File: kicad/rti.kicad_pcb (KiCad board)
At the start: 2 copper layers, 100 x 80 mm, 67 parts, among them J1 28V 250mA, J10 Grove, J2 Trigger, J3 Flash, J4 ICSP, J5 Anodes, J6 Cathodes, J7 Start, J8 Trigger, J9 Flash, Q1 BD140, Q10 BD140, Q11 BD140, Q12 BD140, Q13 BD140, Q14 BD140, Q15 BD140, Q16 BD140, Q2 BD140, Q3 BD140, Q4 BD140, Q5 BD140, Q6 BD140, Q7 BD140, Q8 BD140, Q9 BD140, SW1 Start, SW2 Reset, U1 ATMEGA328P-PU, U2 TPIC6B595, U3 TPIC6B595, U4 LM317T, U5 PC827, U6 LM7805CT, Y1 16MHz

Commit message: WIP. Add pretty picture.
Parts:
- added J11: Reset, Connectors_JST:JST_PH_B3B-PH-K_03x2.00mm_Straight, F.Cu at (235.6, 113.0)
- J2: footprint Connectors_Lumberg:1501_04 -> Connectors_Lumberg:1503_07
- moved J7 10.8 mm to (224.2, 113.0)
- moved U5 3.59 mm to (261.6, 96.5)
- moved C3 2.54 mm to (262.9, 88.9), turned to 90 degrees
- moved C4 2.54 mm to (228.6, 88.9), turned to 90 degrees
- moved G*** 2.01 mm to (215.9, 100.3)
- moved D1 2.01 mm to (211.5, 121.3)
- moved J3 1.27 mm to (245.1, 128.3)
- moved C2 1.27 mm to (174.0, 87.6), turned to 0 degrees
- moved SW2 1.27 mm to (231.1, 124.5)
- moved J8 0.63 mm to (258.4, 113.0)
- moved J9 0.63 mm to (247.0, 113.0)
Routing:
- net /D2: track 72.4 -> 90.0 mm, vias 1 -> 0
- net /D3: track 112.6 -> 98.2 mm
- net Net-(J2-Pad1): track 14.9 -> 28.1 mm
- net Net-(D1-Pad2): track 38.5 -> 28.0 mm
- net /RESET: track 84.8 -> 92.1 mm
- net /D4: track 63.7 -> 69.6 mm, vias 1 -> 0
- net Net-(J2-Pad2): track 19.8 -> 16.1 mm
- net +5V: track 177.9 -> 174.8 mm
- net Net-(R2-Pad2): track 61.4 -> 58.9 mm
- net /D5: track 98.0 -> 100.2 mm, vias 1 -> 0
- net Net-(R3-Pad2): track 56.4 -> 58.5 mm
- net /D8: track 77.9 -> 76.4 mm
- net Net-(J2-Pad3): track 19.7 -> 18.5 mm
- net /D6: track 106.1 -> 106.8 mm
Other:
- board text added: "1"
- board text added: "28V 250mA"
- board text added: "Anodes"
- board text added: "Cathodes"
- board text added: "Flash"
- board text added: "Grove"
- board text added: "ICSP"
- board text added: "Ready"
- board text added: "Reset"
- board text added: "Start"
- board text added: "Trigger"

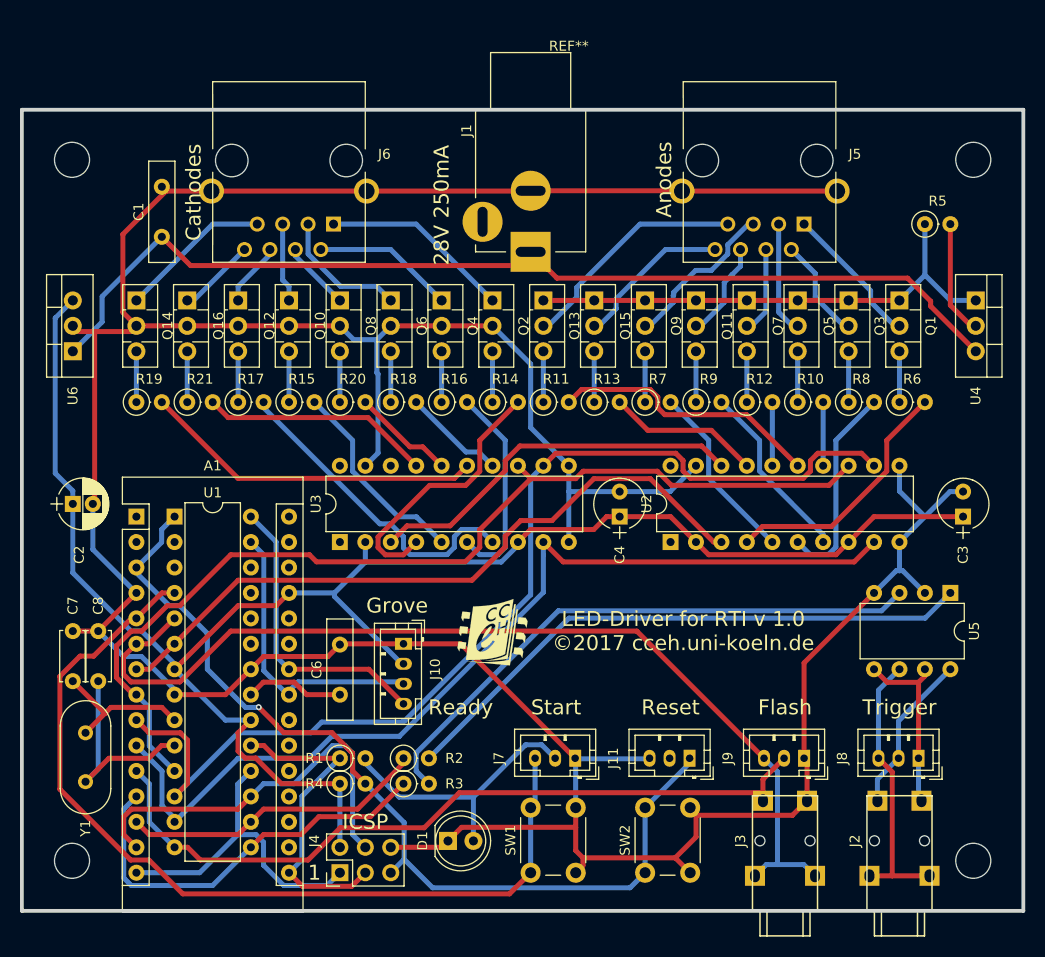
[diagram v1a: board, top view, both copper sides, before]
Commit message: Get rid of Arduino overhead.
Change program to use ATmega port names instead of Arduino.
Add ISP programming in Makefile.
Renumber and move transistors.
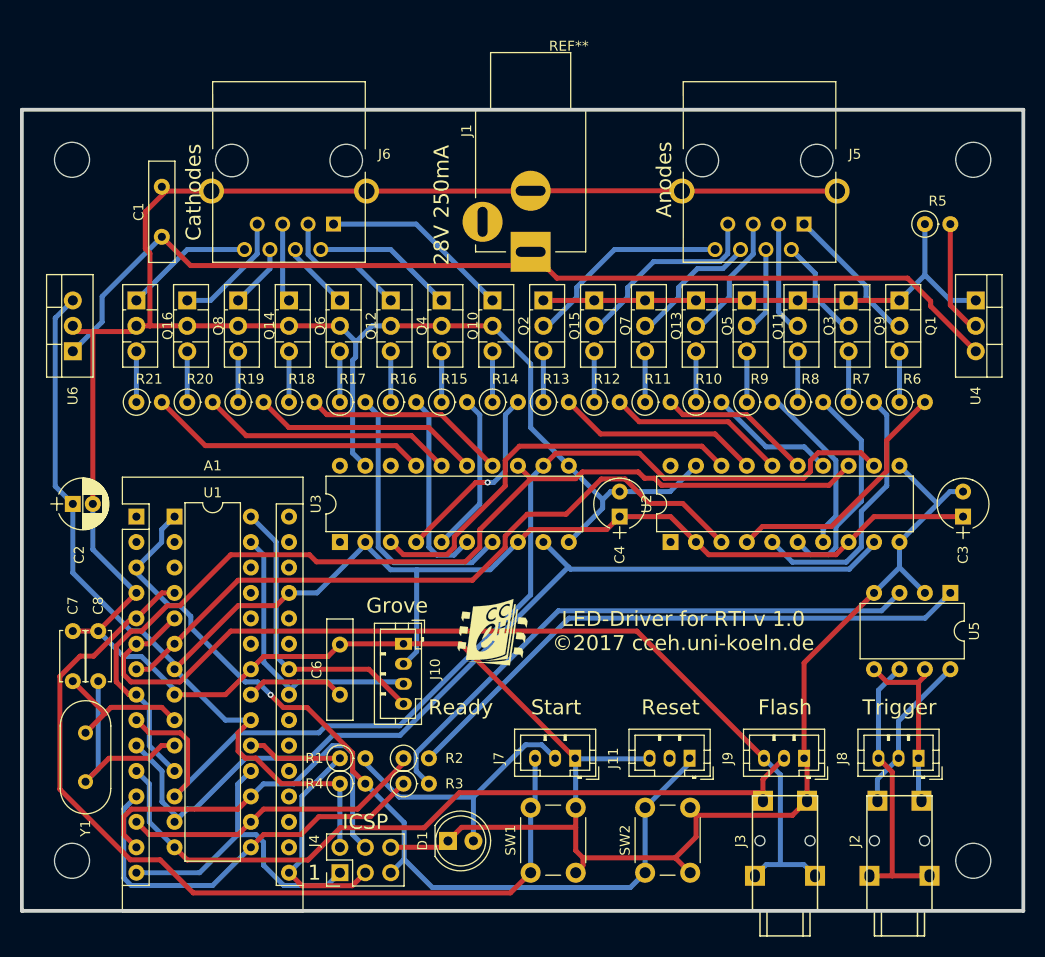
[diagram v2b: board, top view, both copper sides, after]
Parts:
- moved Q9 20.3 mm to (251.5, 67.3)
- moved R7 20.3 mm to (251.5, 77.5)
- moved Q7 15.2 mm to (226.1, 67.3)
- moved Q8 15.2 mm to (185.4, 67.3)
- moved R12 15.2 mm to (226.1, 77.5)
- moved R20 15.2 mm to (185.4, 77.5)
- moved Q10 15.2 mm to (210.8, 67.3)
- moved R15 15.2 mm to (210.8, 77.5)
- moved Q12 10.2 mm to (200.7, 67.3)
- moved Q13 10.2 mm to (231.1, 67.3)
- moved Q14 10.2 mm to (190.5, 67.3)
- moved Q5 10.2 mm to (236.2, 67.3)
- moved Q6 10.2 mm to (195.6, 67.3)
- moved R10 10.2 mm to (236.2, 77.5)
- moved R11 10.2 mm to (231.1, 77.5)
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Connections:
- Q10 pad 1: /Cat4 -> /Cat1
- Q11 pad 2: /An5 -> /An3
- Q12 pad 1: /Cat5 -> /Cat3
- Q13 pad 2: /An6 -> /An5
- Q14 pad 1: /Cat6 -> /Cat5
- Q3 pad 2: /An1 -> /An2
- Q4 pad 1: /Cat1 -> /Cat2
- Q5 pad 2: /An2 -> /An4
- Q6 pad 1: /Cat2 -> /Cat4
- Q7 pad 2: /An3 -> /An6
- Q8 pad 1: /Cat3 -> /Cat6
- Q9 pad 2: /An4 -> /An1
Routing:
- net Net-(R20-Pad2): track 10.3 -> 25.5 mm
- net Net-(R11-Pad2): track 27.2 -> 15.3 mm
- net Net-(R12-Pad2): track 6.35 -> 17.9 mm
- net Net-(R19-Pad2): track 34.2 -> 23.0 mm
- net Net-(R18-Pad2): track 10.3 -> 20.4 mm
- net Net-(R7-Pad2): track 18.2 -> 26.4 mm
- net Net-(R14-Pad2): track 27.0 -> 19.2 mm, vias 0 -> 1
- net Net-(R10-Pad2): track 6.35 -> 12.8 mm
- net /An7: track 15.8 -> 20.9 mm
- net /Cat7: track 7.82 -> 12.9 mm
- net Net-(R13-Pad2): track 15.3 -> 20.4 mm
- net Net-(R21-Pad2): track 23.0 -> 28.0 mm
- net Net-(R17-Pad2): track 32.3 -> 27.9 mm
- net Net-(R15-Pad2): track 20.3 -> 16.1 mm
- net /An5: track 9.74 -> 13.4 mm
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
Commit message: Get rid of Arduino physically. Add case. New board layout.
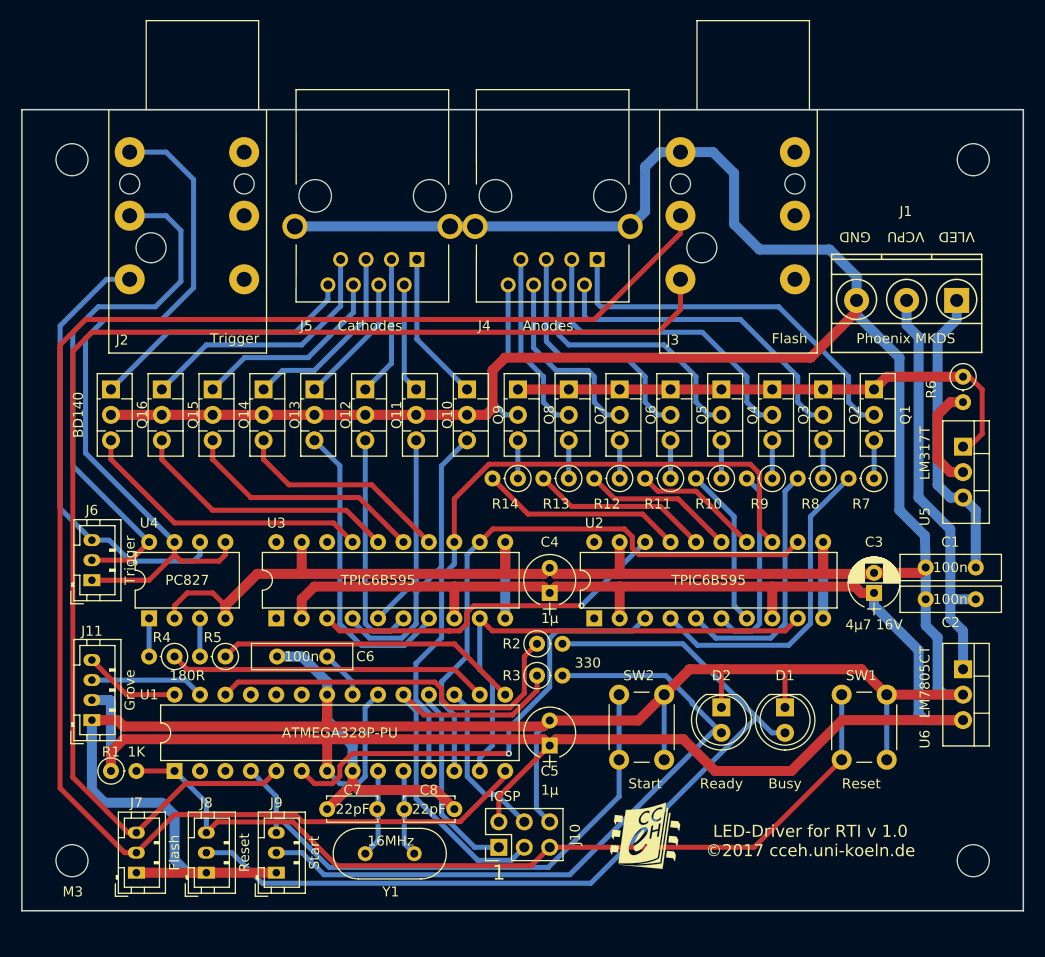
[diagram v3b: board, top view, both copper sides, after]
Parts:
- removed A1: Arduino_Nano_v3.x, Modules:Arduino_Nano
- removed the R14 at (215.9, 77.5)
- removed R15, R16, R17, R18, R19, R20, R21: 0R, Resistors_THT:R_Axial_DIN0207_L6.3mm_D2.5mm_P2.54mm_Vertical
- removed the R5 at (259.1, 59.7)
- removed REF**: EuroBoard_halb_Type-I_100mmX80mm_holes, EuroBoard_Outline:EuroBoard_halb_Type-I_100mmX80mm_holes
- added C2: 100n, Capacitors_THT:C_Disc_D10.0mm_W2.5mm_P5.00mm, F.Cu at (264.2, 97.2)
- added D1: Busy, LEDs:LED_D5.0mm, F.Cu at (245.1, 108.0)
- added M3: MountingHole_3.2mm_M3_DIN965, Mounting_Holes:MountingHole_3.2mm_M3, F.Cu at (173.9, 123.3)
- added M3_1: MountingHole_3.2mm_M3_DIN965, Mounting_Holes:MountingHole_3.2mm_M3, F.Cu at (173.9, 53.3)
- added M3_2: MountingHole_3.2mm_M3_DIN965, Mounting_Holes:MountingHole_3.2mm_M3, F.Cu at (263.9, 53.3)
- added M3_3: MountingHole_3.2mm_M3_DIN965, Mounting_Holes:MountingHole_3.2mm_M3, F.Cu at (263.9, 123.3)
- added R2: 330, Resistors_THT:R_Axial_DIN0207_L6.3mm_D2.5mm_P2.54mm_Vertical, F.Cu at (220.3, 101.6)
- added R6: 6R2 0W25, Resistors_THT:R_Axial_DIN0207_L6.3mm_D2.5mm_P2.54mm_Vertical, F.Cu at (262.9, 74.9)
- C7, C8: value 15pF -> 22pF
- J1: value 28V 250mA -> Phoenix MKDS; footprint Connectors_Anonymous:HEBG9_21 -> Connectors_Terminal_Blocks:TerminalBlock_Pheonix_MKDS1.5-3pol
- J2, J3: footprint Connectors_Lumberg:1503_07 -> Connectors_Neutrik:NRJ6HF
- R3: renamed from R1; value 1K -> 330
- moved J2 106.1 mm to (186.9, 48.3), turned to 0 degrees
- moved U6 94.4 mm to (262.9, 104.1), turned to 270 degrees
- moved C1 87.7 mm to (264.2, 94.0), turned to 180 degrees
- moved J6 84.4 mm to (175.9, 95.2), turned to 90 degrees
- moved C3 80.5 mm to (254.0, 96.5), turned to 90 degrees
- moved J3 80.1 mm to (241.9, 48.3), turned to 0 degrees
- moved U4 80.1 mm to (181.6, 99.1), turned to 90 degrees
- moved J7 67.6 mm to (180.3, 124.5), turned to 90 degrees
- moved J8 49.6 mm to (187.3, 124.5), turned to 90 degrees
- moved J1 46.6 mm to (262.3, 67.3), turned to 180 degrees
- moved C4 42.0 mm to (221.6, 96.5)
- moved C8 39.8 mm to (212.1, 118.1), turned to 180 degrees
- moved R14 38.9 mm to (218.4, 85.1), turned to 180 degrees
- moved J11 32.0 mm to (175.9, 109.2), turned to 90 degrees
- moved J9 32.0 mm to (194.3, 124.5), turned to 90 degrees
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- renumbered C2 to C3, C3 to C4, C4 to C5, D1 to D2, J4 to J10, J10 to J11, J5 to J4, J6 to J5, J8 to J6, J9 to J7, J11 to J8, J7 to J9, Q4 to Q11, Q6 to Q13, Q8 to Q15, Q9 to Q2, Q11 to Q4, Q13 to Q6, Q15 to Q8, Q2 to Q9, R4 to R1, R6 to R14, R2 to R4, R3 to R5, SW2 to SW1, SW1 to SW2, U5 to U4, U4 to U5
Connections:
- C1 pad 1: /VIN -> /VINLED
- J1 pad 1: /VIN -> /VINLED
- J1 pad 2: GND -> /VINCPU
- J1 pad 3: (no net) -> GND
- J10 pad 5: /RESET -> /~RESET
- J8 pad 1: /RESET -> GND
- J8 pad 2: (no net) -> Net-(D1-Pad2)
- J8 pad 3: GND -> /~RESET
- Q11 pad 3: Net-(Q4-Pad3) -> Net-(Q11-Pad3)
- Q13 pad 3: Net-(Q6-Pad3) -> Net-(Q13-Pad3)
- Q15 pad 3: Net-(Q8-Pad3) -> Net-(Q15-Pad3)
- Q2 pad 3: Net-(Q9-Pad3) -> Net-(Q2-Pad3)
- Q4 pad 3: Net-(Q11-Pad3) -> Net-(Q4-Pad3)
- Q6 pad 3: Net-(Q13-Pad3) -> Net-(Q6-Pad3)
- Q8 pad 3: Net-(Q15-Pad3) -> Net-(Q8-Pad3)
- Q9 pad 3: Net-(Q2-Pad3) -> Net-(Q9-Pad3)
- R1 pad 2: /RESET -> /~RESET
- R10 pad 1: Net-(Q5-Pad3) -> Net-(Q4-Pad3)
- R11 pad 1: Net-(Q13-Pad3) -> Net-(Q5-Pad3)
- R12 pad 1: Net-(Q7-Pad3) -> Net-(Q6-Pad3)
- R13 pad 1: Net-(Q15-Pad3) -> Net-(Q7-Pad3)
- R14 pad 1: Net-(Q1-Pad3) -> Net-(Q8-Pad3)
- R14 pad 2: Net-(R6-Pad2) -> Net-(R14-Pad2)
- R7 pad 1: Net-(Q9-Pad3) -> Net-(Q1-Pad3)
- R8 pad 1: Net-(Q3-Pad3) -> Net-(Q2-Pad3)
- R9 pad 1: Net-(Q11-Pad3) -> Net-(Q3-Pad3)
- SW1 pad 1: /RESET -> GND
- SW1 pad 2: GND -> /~RESET
- SW2 pad 1: /D2 -> GND
- SW2 pad 2: GND -> /D2
- U1 pad 1: /RESET -> /~RESET
- U1 pad 26: (no net) -> /A3
- U2 pad 14: Net-(R10-Pad2) -> Net-(R11-Pad2)
- U2 pad 15: Net-(R11-Pad2) -> Net-(R12-Pad2)
- U2 pad 16: Net-(R12-Pad2) -> Net-(R13-Pad2)
- U2 pad 17: Net-(R13-Pad2) -> Net-(R14-Pad2)
- U2 pad 4: Net-(R6-Pad2) -> Net-(R7-Pad2)
- U2 pad 5: Net-(R7-Pad2) -> Net-(R8-Pad2)
- U2 pad 6: Net-(R8-Pad2) -> Net-(R9-Pad2)
- U2 pad 7: Net-(R9-Pad2) -> Net-(R10-Pad2)
- U3 pad 14: Net-(R18-Pad2) -> Net-(Q13-Pad3)
- U3 pad 15: Net-(R19-Pad2) -> Net-(Q14-Pad3)
- U3 pad 16: Net-(R20-Pad2) -> Net-(Q15-Pad3)
- U3 pad 17: Net-(R21-Pad2) -> Net-(Q16-Pad3)
- U3 pad 4: Net-(R14-Pad2) -> Net-(Q9-Pad3)
- U3 pad 5: Net-(R15-Pad2) -> Net-(Q10-Pad3)
- U3 pad 6: Net-(R16-Pad2) -> Net-(Q11-Pad3)
- U3 pad 7: Net-(R17-Pad2) -> Net-(Q12-Pad3)
- U5 pad 3: /VIN -> /VINLED
- U6 pad 1: /VIN -> /VINCPU
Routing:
- net GND: track 385.6 -> 505.4 mm
- net /VIN: track 102.6 -> 0.00 mm
- net /RESET: track 90.6 -> 0.00 mm, vias 1 -> 0
- net Net-(D1-Pad2): track 0.00 -> 89.0 mm
- net /~RESET: track 0.00 -> 87.9 mm
- net /D8: track 76.4 -> 164.2 mm
- net Net-(R4-Pad2): track 58.9 -> 3.81 mm
- net Net-(J2-Pad3): track 18.5 -> 73.3 mm
- net Net-(R5-Pad2): track 58.5 -> 3.81 mm
- net /D6: track 106.2 -> 59.5 mm
- net /D7: track 94.2 -> 49.1 mm
- net /VINCPU: track 0.00 -> 41.7 mm
- net Net-(D2-Pad2): track 28.0 -> 69.3 mm
- net +5V: track 174.9 -> 215.1 mm
- net /A3: track 0.00 -> 38.1 mm
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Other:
- rule trace_min: 0.2 -> 0.1
- rule via_min_drill: 0.3 -> 0.2
- rule via_min_size: 0.4 -> 0.45
- board text added: "GND"
- board text added: "VCPU"
- board text added: "VLED"
- board text removed: "28V 250mA"
- board text removed: "Anodes"
- board text removed: "Cathodes"
- board text removed: "Flash"
- board text removed: "Grove"
- board text removed: "ICSP"
- board text removed: "Ready"
- board text removed: "Reset"
- board text removed: "Start"
- board text removed: "Trigger"

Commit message: Add BOM.
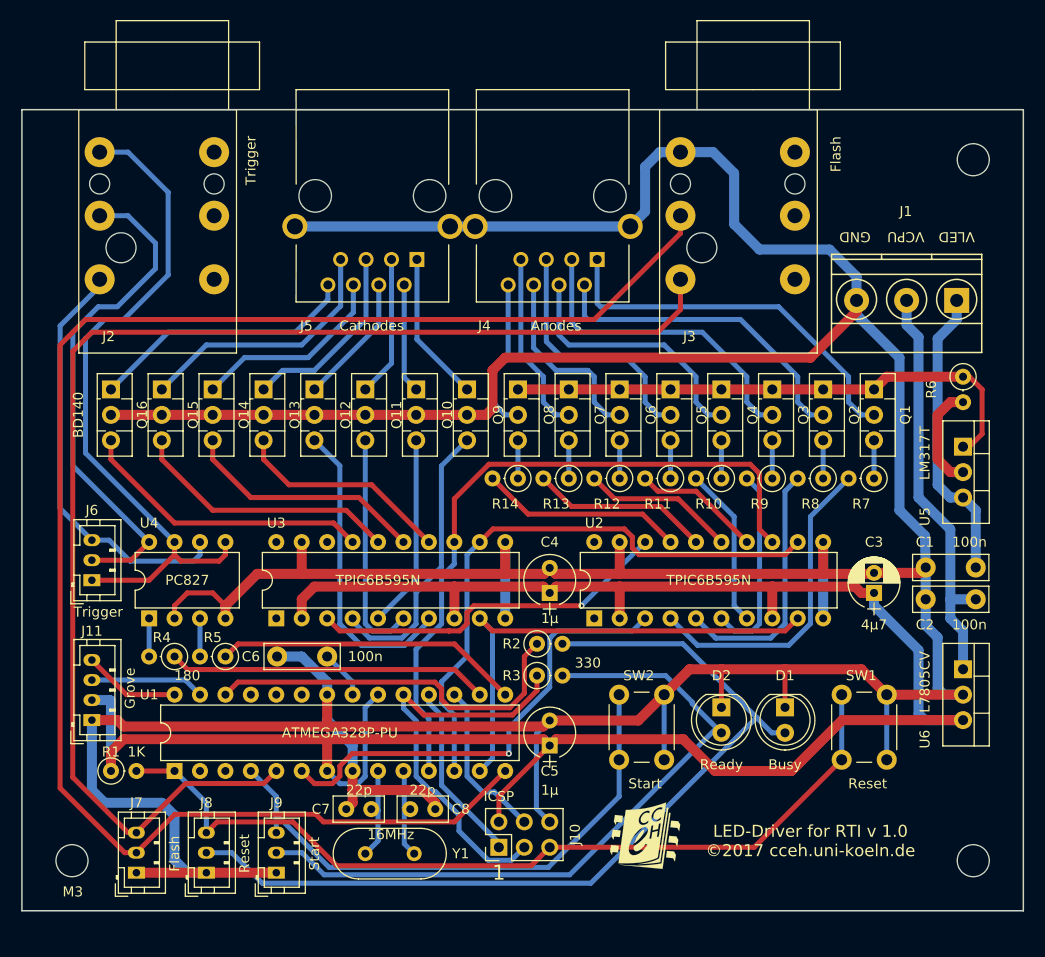
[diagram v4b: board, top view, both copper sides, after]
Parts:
- removed M3_1: MountingHole_3.2mm_M3_DIN965, Mounting_Holes:MountingHole_3.2mm_M3
- C1, C2, C6: footprint Capacitors_THT:C_Disc_D10.0mm_W2.5mm_P5.00mm -> Capacitors_THT:C_Disc_D7.5mm_W2.5mm_P5.00mm
- C3: value 4µ7 16V -> 4µ7
- C7, C8: value 22pF -> 22p; footprint Capacitors_THT:C_Disc_D5.0mm_W2.5mm_P5.00mm -> Capacitors_THT:C_Disc_D5.0mm_W2.5mm_P2.50mm
- D1: value Busy -> Red
- D2: value Ready -> Green
- J10: value ICSP -> Header 2x3
- J11: value Grove -> JST PH 4
- J2: value Trigger -> Neutrik NRJ6HF
- J3: value Flash -> Neutrik NRJ6HF
- J4: value Anodes -> MEBP 8-8G
- J5: value Cathodes -> MEBP 8-8G
- J6: value Trigger -> JST PH 3
- J7: value Flash -> JST PH 3
- J8: value Reset -> JST PH 3
- J9: value Start -> JST PH 3
- R4, R5: value 180R -> 180
- R6: value 6R2 0W25 -> 6R2
- SW1: value Reset -> Switch
- SW2: value Start -> Switch
- U2, U3: value TPIC6B595 -> TPIC6B595N
- U6: value LM7805CT -> L7805CV
- moved J2 3.00 mm to (183.9, 48.3)
- moved C7 1.91 mm to (201.3, 118.1)
- moved C8 1.91 mm to (210.2, 118.1)
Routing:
- net Net-(J2-Pad3): track 73.3 -> 69.7 mm
- net Net-(J2-Pad2): track 54.3 -> 50.7 mm
- net GND: track 505.4 -> 502.9 mm
- net Net-(J2-Pad1): track 44.8 -> 43.2 mm
- net /D12: track 19.5 -> 18.1 mm
- net Net-(C8-Pad2): track 8.70 -> 9.35 mm
- net Net-(C7-Pad2): track 8.95 -> 9.55 mm
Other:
- board text added: "Anodes"
- board text added: "Busy"
- board text added: "Cathodes"
- board text added: "Flash"
- board text added: "Grove"
- board text added: "ICSP"
- board text added: "Ready"
- board text added: "Reset"
- board text added: "Start"
- board text added: "Trigger"

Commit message: WIP. Use ceramic C and R arrays.
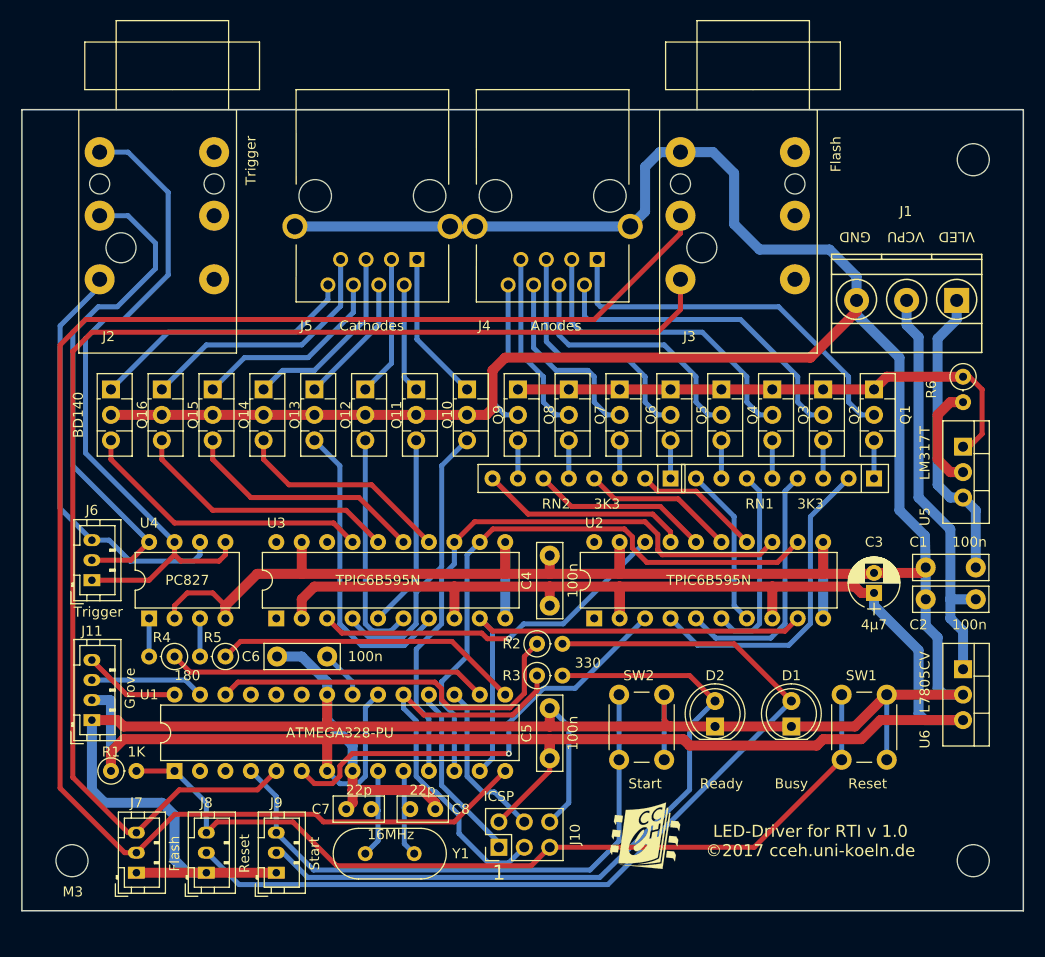
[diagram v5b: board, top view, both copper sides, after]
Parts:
- removed R10, R11, R12, R13, R14, R7, R8, R9: 3K3, Resistors_THT:R_Axial_DIN0207_L6.3mm_D2.5mm_P2.54mm_Vertical
- added RN1: 3K3, Resistors_THT:R_Array_SIP8, F.Cu at (254.0, 85.1)
- added RN2: 3K3, Resistors_THT:R_Array_SIP8, F.Cu at (233.7, 85.1)
- C4, C5: value 1µ -> 100n; footprint Capacitors_THT:CP_Radial_Tantal_D5.0mm_P2.50mm -> Capacitors_THT:C_Disc_D7.5mm_W2.5mm_P5.00mm
- J2, J3: value Neutrik NRJ6HF -> NRJ6HF
- U1: value ATMEGA328P-PU -> ATMEGA328-PU
- moved D1 2.01 mm to (245.7, 109.9), turned to 90 degrees
- moved D2 2.01 mm to (238.1, 109.9), turned to 90 degrees
- moved C4 1.27 mm to (221.6, 97.8)
- moved C5 1.27 mm to (221.6, 113.0)
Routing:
- net /D5: track 69.0 -> 60.4 mm
- net +5V: track 215.1 -> 219.6 mm
- net Net-(D1-Pad2): track 89.0 -> 92.6 mm
- net Net-(D2-Pad2): track 69.3 -> 72.1 mm
- net /D4: track 46.6 -> 44.0 mm
- net /D2: track 56.7 -> 58.8 mm
- net GND: track 502.9 -> 504.6 mm
- net /D6: track 59.5 -> 60.1 mm
- net Net-(RN2-Pad8): track 20.4 -> 21.0 mm
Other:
- net class HC2HC added: clearance 0.2, trace_width 0.5, via_dia 0.6, via_drill 0.4
